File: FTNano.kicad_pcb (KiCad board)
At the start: 4 copper layers, 17.8 x 43.2 mm, 39 parts, among them CN1 AFC10-S04QCA-00, J1 Conn_01x15_Pin, J2 Conn_01x15_Pin, Q1 2N7002DW-7-F, SW1 GT-TC029B-H020-L1N, U1 ATmega328P-MU, U2 CH340K, U3 ME6214A50M3G, U4 ME6211C33R5G, X1 CSTCE16M0V53-R0

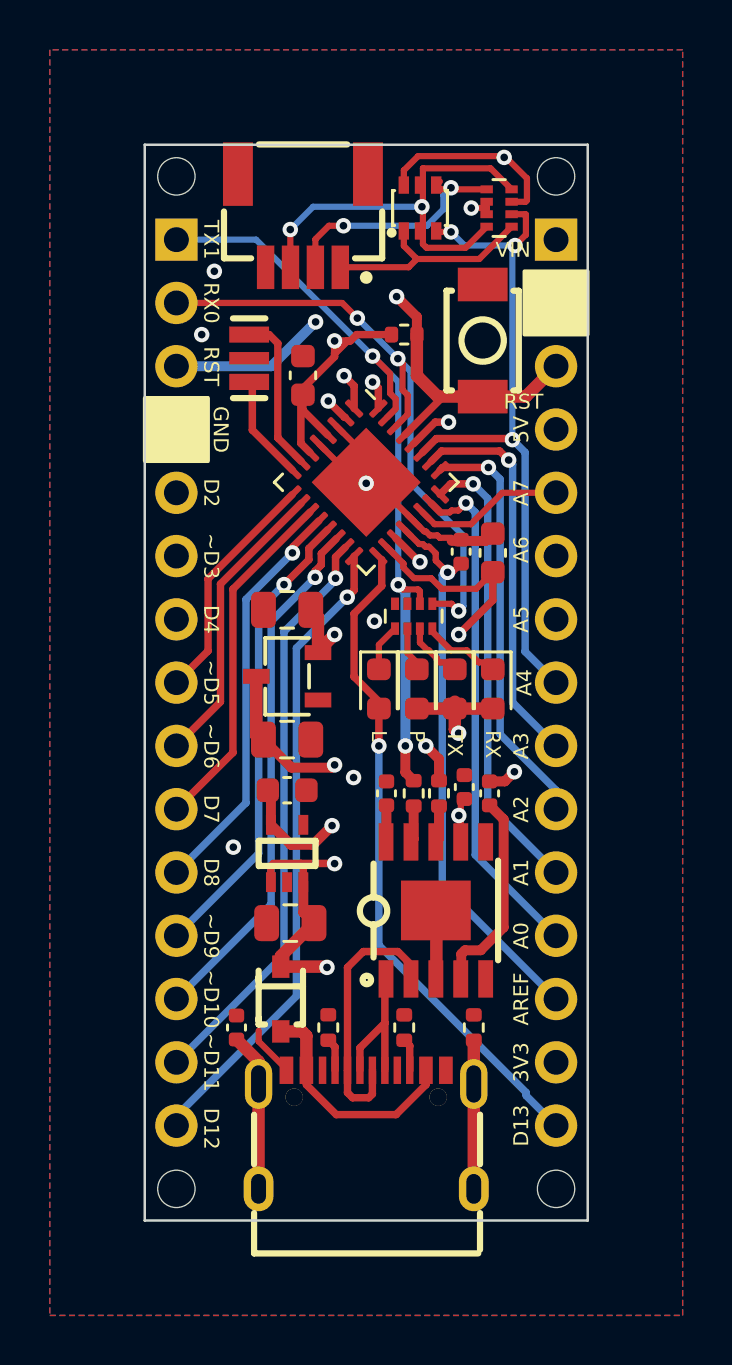
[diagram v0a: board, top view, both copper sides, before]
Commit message: fix qwiic, add tvs
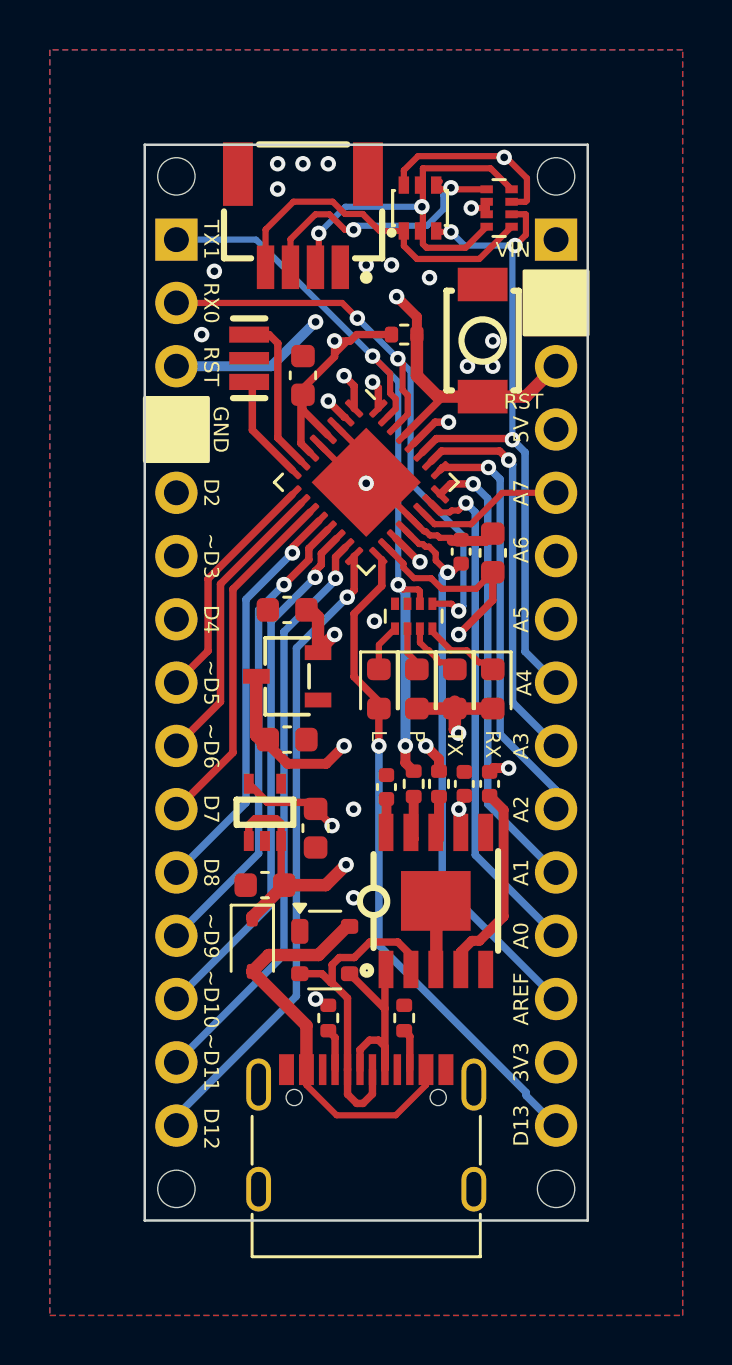
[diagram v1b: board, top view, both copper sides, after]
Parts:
- removed C10: 4.7u, Capacitor_SMD:C_0402_1005Metric
- removed R6: 5.1k, Resistor_SMD:R_0402_1005Metric
- removed USB1: TYPE-C 16PIN 2MD(073), nano:USB-C-SMD_TYPE-C-6PIN-2MD-073
- added J3: USB_C_Receptacle_USB2.0_16P, Connector_USB:USB_C_Receptacle_G-Switch_GT-USB-7010ASV, F.Cu at (182.9, 115.8)
- added TV1: PRTR5V0U2X, Package_TO_SOT_SMD:SOT-143, F.Cu at (181.2, 107.3)
- C6, C7, C8: footprint Capacitor_SMD:C_0805_2012Metric -> Capacitor_SMD:C_0603_1608Metric
- D1: value 1N5819WS S4 -> 1N5819WS; footprint nano:SOD-323_L1.6-W1.3-LS2.7-RD -> Diode_SMD:D_SOD-323
- R4: value 1M -> 5.1k
- moved R4 5.85 mm to (181.4, 110.0)
- moved R5 3.07 mm to (184.4, 110.0), turned to 90 degrees
- moved D1 2.44 mm to (178.3, 107.1)
- moved C9 1.91 mm to (180.8, 102.4), turned to 90 degrees
- moved U4 1.88 mm to (178.8, 101.7)
- moved C8 1.83 mm to (178.8, 104.6)
- moved C5 0.38 mm to (187.8, 100.6)
- moved R1 0.38 mm to (184.8, 100.6)
- moved R2 0.38 mm to (185.8, 100.6)
- moved U2 0.38 mm to (185.7, 105.3)
- moved C3 0.25 mm to (183.7, 100.7)
- moved C4 0.13 mm to (186.8, 100.6)
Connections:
- CN1 pad 1: /SCL -> GND
- CN1 pad 2: /SDA -> +3.3V
- CN1 pad 3: +3.3V -> /SDA
- CN1 pad 4: GND -> /SCL
- R5 pad 1: GND -> Net-(J3-CC2)
- R5 pad 2: Net-(USB1-CC1) -> GND
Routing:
- net VBUS: track 9.44 -> 16.5 mm
- net Net-(C10-Pad1): track 6.36 -> 0.00 mm
- net /SCL: track 8.89 -> 13.7 mm
- net Net-(J3-CC1): track 5.97 -> 1.67 mm
- net DN: track 10.5 -> 13.8 mm
- net DP: track 6.28 -> 9.12 mm
- net GND: track 16.3 -> 14.2 mm, vias 6 -> 17
- net Net-(J3-CC2): track 0.00 -> 1.65 mm
- net /SDA: track 10.1 -> 11.6 mm
- net Net-(USB1-CC1): track 1.32 -> 0.00 mm
- net Net-(USB1-CC2): track 1.30 -> 0.00 mm
- net +5V: track 44.6 -> 43.6 mm, vias 8 -> 7
- net Net-(U2-~{DTR}): track 8.00 -> 8.81 mm
- net +3.3V: track 61.8 -> 61.2 mm
- net RST: track 48.7 -> 48.2 mm

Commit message: fix led
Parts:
- removed U3: ME6214A50M3G, nano:SOT-23-3_L2.9-W1.6-P1.90-LS2.8-BR
- added U5: SPX3819M5-L-5-0, Package_TO_SOT_SMD:SOT-23-5, F.Cu at (179.7, 96.8)
- RN1, RN2: value 2.2k -> 4.7k
- moved U4 2.48 mm to (181.2, 102.3)
- moved C8 2.37 mm to (181.2, 104.8), turned to 180 degrees
- moved C9 1.96 mm to (178.9, 102.0)
- moved C6 0.74 mm to (179.7, 99.5), turned to 180 degrees
- moved C7 0.41 mm to (179.5, 94.0)
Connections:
- C6 pad 1: VDC -> GND
- C6 pad 2: GND -> VDC
- C7 pad 1: +5V -> GND
- C7 pad 2: GND -> +5V
- TV1 pad 1: unconnected-(TV1-GND-Pad1) -> GND
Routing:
- net GND: track 14.2 -> 23.6 mm, vias 17 -> 15
- net +5V: track 43.6 -> 47.3 mm
- net +3.3V: track 61.2 -> 59.8 mm
- net VDC: track 31.6 -> 32.6 mm
